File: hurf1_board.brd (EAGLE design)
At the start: 59 x 59 mm, 41 parts, among them IC1 STM32F10XCXT6, J1 0R, J2 0R, X1 MINI-USB-32005-201, Y1 8MHz

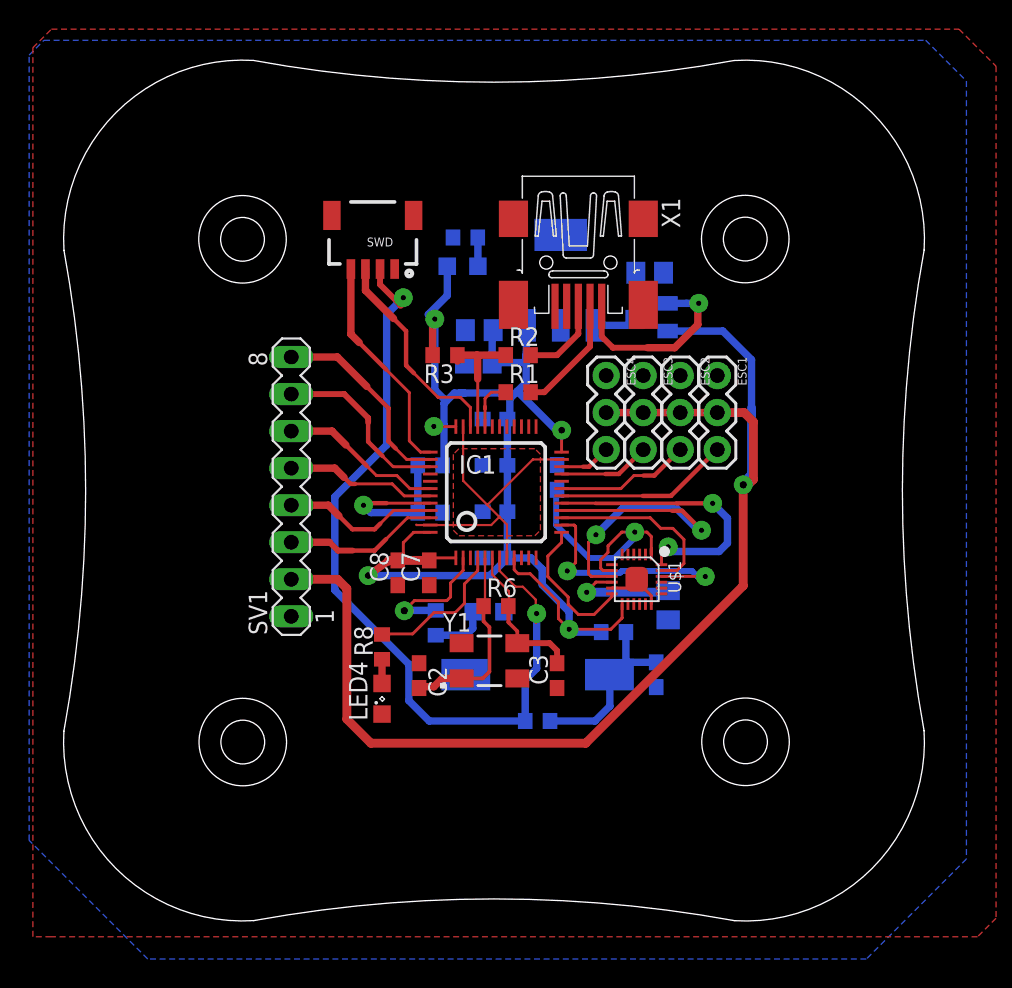
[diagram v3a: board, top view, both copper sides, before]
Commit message: Final touches to board -schematic w1 (updated)  *RC_IN port package updated from DIL -> JST-SH -board w1s1(updated)  *Schematics changes applied  *General check successful  *Signs and Logos added -Status: RTF
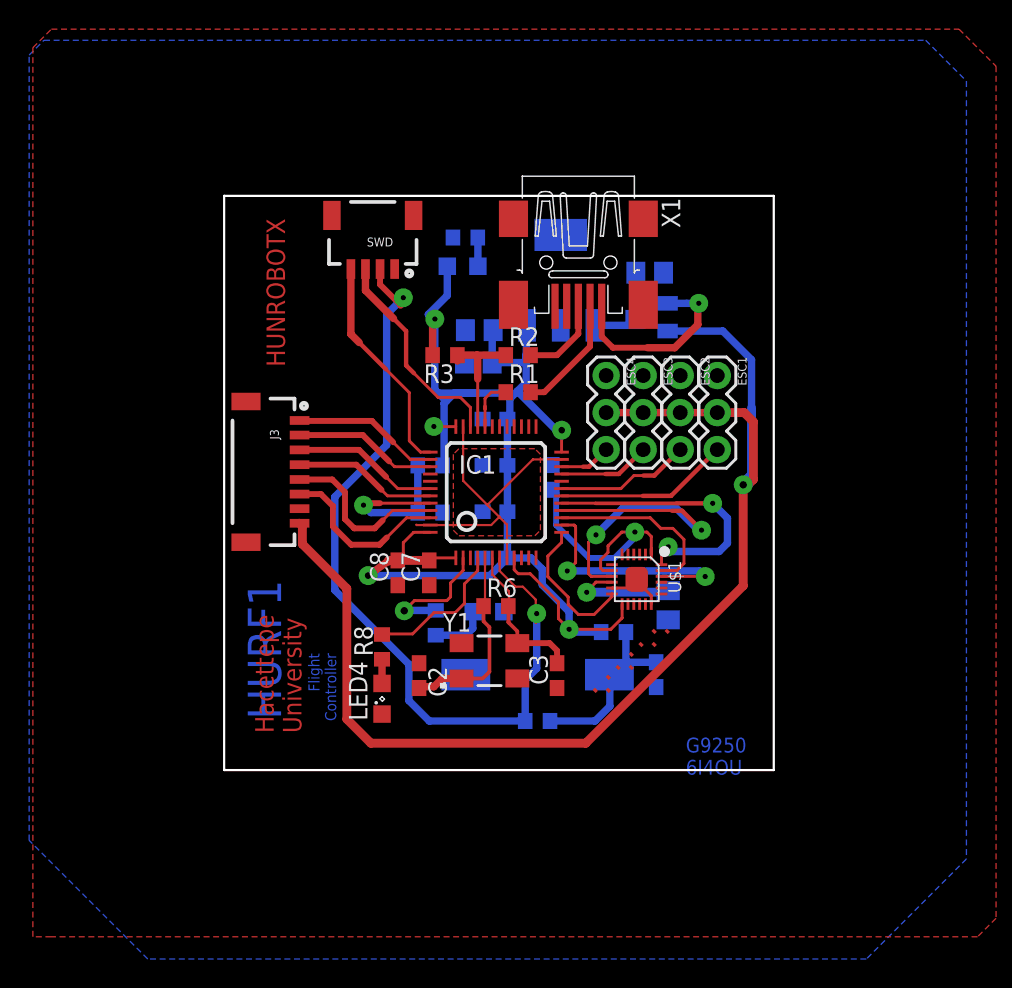
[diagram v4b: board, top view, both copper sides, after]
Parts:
- removed SV1: RC_DATA, con-lstb:MA08-1
- added J3: (no value), SparkFun-Connectors:1X08_1MM_RA
- moved C6 0.32 mm to (3.87, 1.02)
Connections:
- net GND: now also J3.7; no longer SV1.1
- net RC_IN1: now also J3.6; no longer SV1.3
- net RC_IN2: now also J3.5; no longer SV1.4
- net RC_IN3: now also J3.4; no longer SV1.5
- net RC_IN4: now also J3.3; no longer SV1.6
- net RC_IN5: now also J3.2; no longer SV1.7
- net RC_IN6: now also J3.1; no longer SV1.8
- net UNREG_5V: now also J3.8; no longer SV1.2
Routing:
- net RC_IN6: track 13.8 -> 10.1 mm
- net 3.3V: track 103.8 -> 106.8 mm
- net RC_IN5: track 12.5 -> 9.86 mm
- net UNREG_5V: track 83.0 -> 84.7 mm
- net RC_IN1: track 10.7 -> 12.0 mm
- net RC_IN2: track 10.8 -> 11.9 mm
- net RC_IN4: track 11.2 -> 10.1 mm
- net RC_IN3: track 10.4 -> 9.85 mm
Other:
- board size 59 x 59 mm -> 37.7 x 39.4 mm
- board text added: "."
- board text added: "Flight Controller"
- board text added: "G9250 6I4OU"
- board text added: "HUNROBOTX"
- board text added: "HURF1"
- board text added: "Hacettepe University"

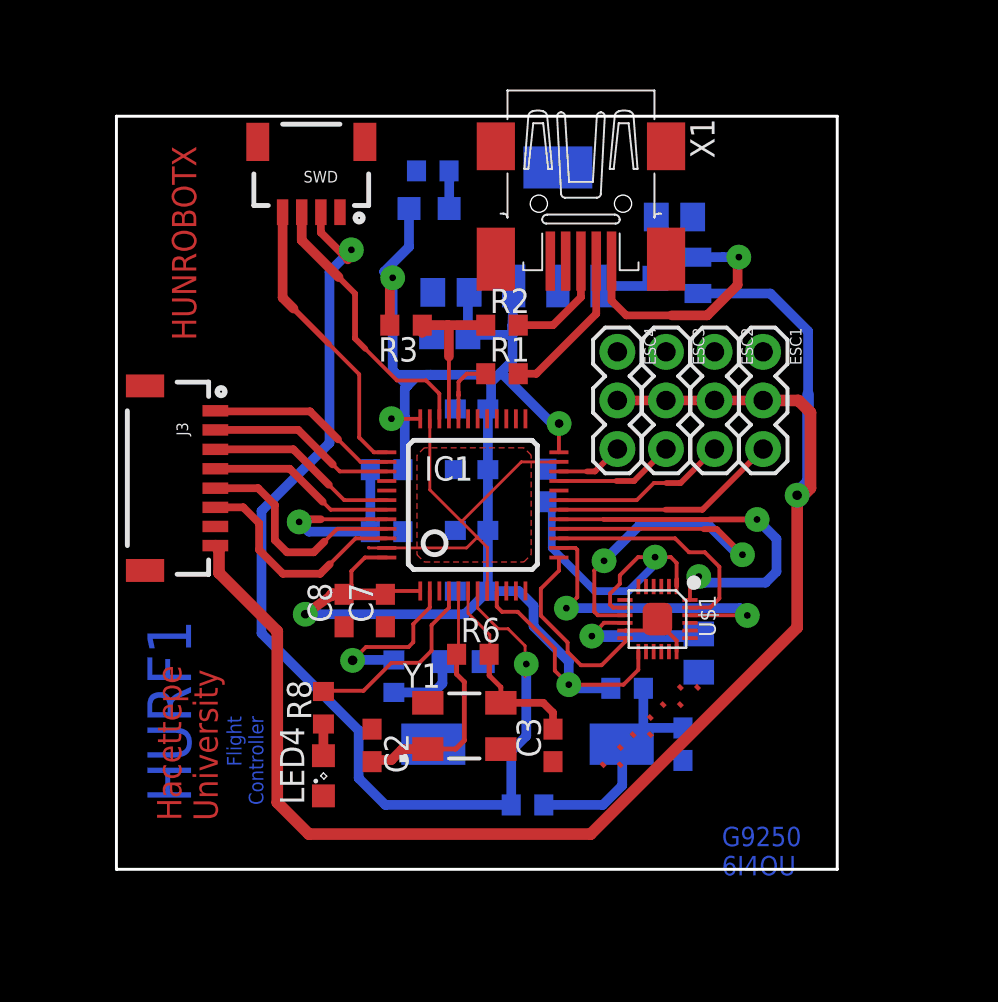
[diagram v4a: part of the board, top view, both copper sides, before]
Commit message: Drills added , gerber out -schematic w1 (updated) -board w1s1 (updated)  *Corner Mount holes added (3mm)  *Board corners rounded  *Signs and logos rearrenged -Status : RTF =gerber_out files added
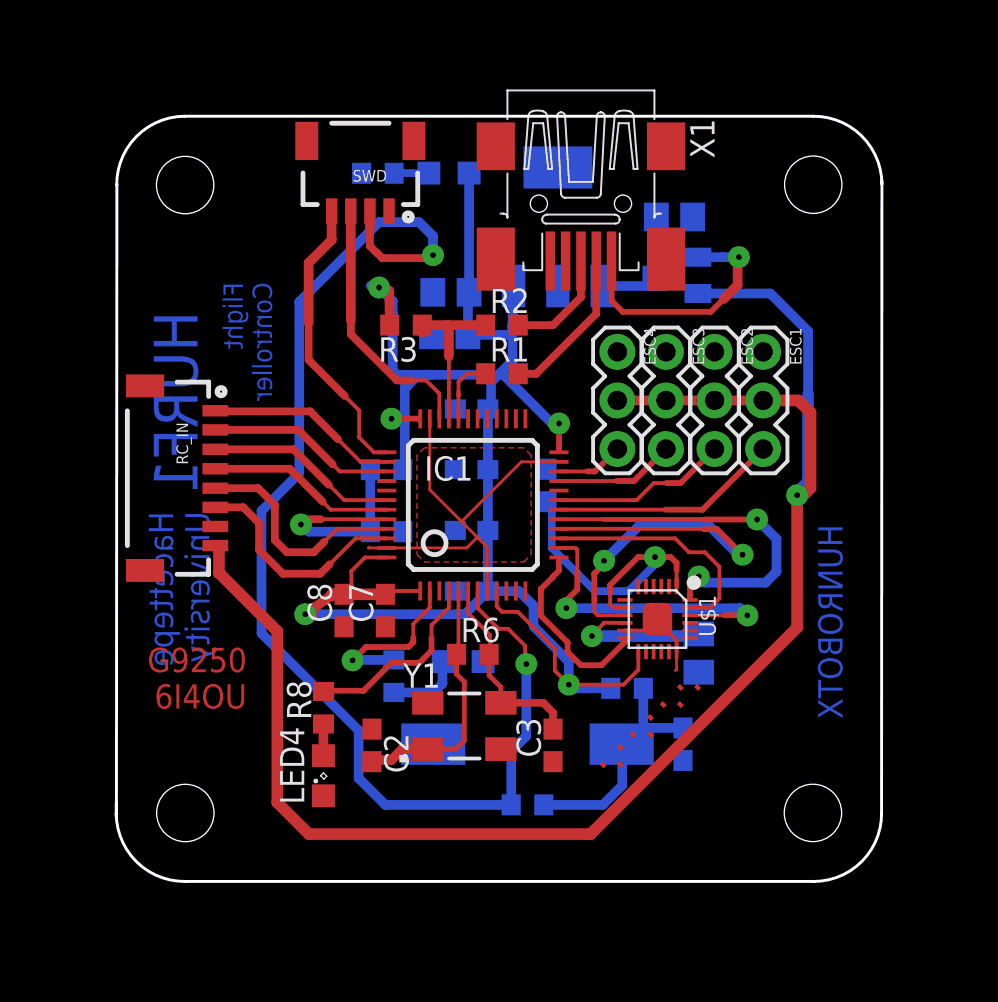
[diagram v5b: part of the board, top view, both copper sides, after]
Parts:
- added H1, H2, H3, H4: MOUNT-HOLE3.0, holes:3,0
- moved R7 2.87 mm to (-4.97, 17.3)
- moved SWD 2.57 mm to (-5.88, 15.4)
- moved LED5 2.13 mm to (-1.24, 17.3), turned to 180 degrees
- renumbered J3 to RC_IN
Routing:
- net NRST: track 58.0 -> 64.7 mm
- net OSC_IN: track 15.2 -> 18.6 mm
- net 3.3V: track 106.8 -> 108.8 mm
- net OSC_OUT: track 12.3 -> 13.3 mm
- net GND: track 26.1 -> 27.1 mm
- net SWDIO: track 14.7 -> 13.7 mm
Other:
- board size 37.7 x 39.4 mm -> 40 x 40 mm
